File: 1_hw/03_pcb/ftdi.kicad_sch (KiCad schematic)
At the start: 32 parts, among them U4 93LC56BT-I_OT, Y3 12 MHz

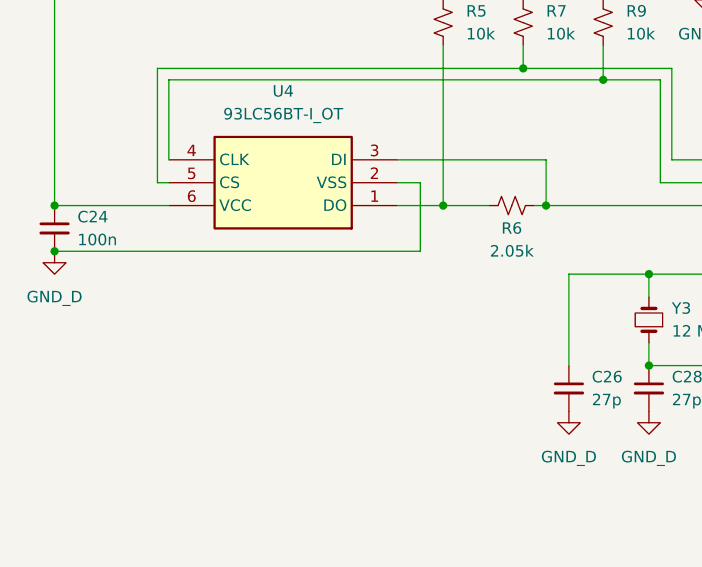
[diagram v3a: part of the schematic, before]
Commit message: FEAT: Added Analog Stage 2 to Schematic. Some additional symbols (Pot, SPDT Analog MUX, etc.) added to Project.
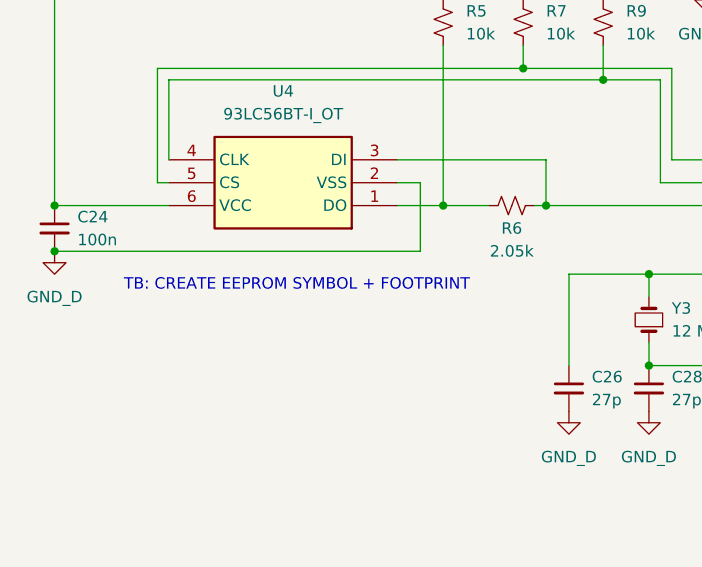
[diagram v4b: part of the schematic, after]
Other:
- note added: "TB: CREATE EEPROM SYMBOL + FOOTPRINT"
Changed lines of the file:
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@@
 		)
 	)
+	(text "TB: CREATE EEPROM SYMBOL + FOOTPRINT"
+		(exclude_from_sim no)
+		(at 71.374 134.62 0)
+		(effects
+			(font
+				(size 1.27 1.27)
+			)
+		)
+	)
 	(text "FTDI PIN 16: UART_FTDI_TXD\nFTDI PIN 17: UART_TFDI_RXD\n(LINES FLIPPED TO MCU)"
 		(exclude_from_sim no)
@@
 			)
 		)
-		(property "Description" ""
+		(property "Description" "Two pin crystal, small symbol"
 			(at 110.49 138.43 0)
 			(effects
@@
 			)
 		)
-		(property "Description" ""
+		(property "Description" "Unpolarized capacitor, small symbol"
 			(at 44.45 128.27 0)
 			(effects
@@
 			)
 		)
-		(property "Description" ""
+		(property "Description" "Unpolarized capacitor, small symbol"
 			(at 210.82 34.29 0)
 			(effects
@@
 			)
 		)
-		(property "Description" ""
+		(property "Description" "Unpolarized capacitor, small symbol"
 			(at 113.03 38.1 0)
 			(effects
@@
 			)
 		)
-		(property "Description" ""
+		(property "Description" "Unpolarized capacitor, small symbol"
 			(at 118.11 63.5 0)
 			(effects
@@
 			)
 		)
-		(property "Description" ""
+		(property "Description" "Light emitting diode"
 			(at 233.68 64.77 0)
 			(effects
@@
 			)
 		)
-		(property "Description" ""
+		(property "Description" "Unpolarized capacitor, small symbol"
 			(at 102.87 38.1 0)
 			(effects
@@
 			)
 		)
-		(property "Description" ""
+		(property "Description" "Unpolarized capacitor, small symbol"
 			(at 180.34 34.29 0)
 			(effects
@@
 			)
 		)
-		(property "Description" ""
+		(property "Description" "Unpolarized capacitor, small symbol"
 			(at 241.3 34.29 0)
 			(effects
@@
 			)
 		)
-		(property "Description" ""
+		(property "Description" "Unpolarized capacitor, small symbol"
 			(at 220.98 34.29 0)
 			(effects
@@
 			)
 		)
-		(property "Description" ""
+		(property "Description" "Unpolarized capacitor, small symbol"
 			(at 123.19 38.1 0)
 			(effects
@@
 			)
 		)
-		(property "Description" ""
+		(property "Description" "Unpolarized capacitor, small symbol"
 			(at 110.49 146.05 0)
 			(effects
@@
 			)
 		)
-		(property "Description" ""
+		(property "Description" "Inductor, small symbol"
 			(at 85.09 34.29 0)
 			(effects
@@
 			)
 		)
-		(property "Description" ""
+		(property "Description" "Unpolarized capacitor, small symbol"
 			(at 92.71 38.1 0)
 			(effects
@@
 			)
 		)
-		(property "Description" ""
+		(property "Description" "Unpolarized capacitor, small symbol"
 			(at 101.6 146.05 0)
 			(effects
@@
 			)
 		)
-		(property "Description" ""
+		(property "Description" "Inductor, small symbol"
 			(at 97.79 31.75 0)
 			(effects
@@
 			)
 		)
-		(property "Description" ""
+		(property "Description" "Unpolarized capacitor, small symbol"
 			(at 200.66 34.29 0)
 			(effects
@@
 			)
 		)
-		(property "Description" ""
+		(property "Description" "Unpolarized capacitor, small symbol"
 			(at 190.5 34.29 0)
 			(effects
@@
 			)
 		)
-		(property "Description" ""
+		(property "Description" "Light emitting diode"
 			(at 223.52 64.77 0)
 			(effects
@@
 			)
 		)
-		(property "Description" ""
+		(property "Description" "Unpolarized capacitor, small symbol"
 			(at 231.14 34.29 0)
 			(effects

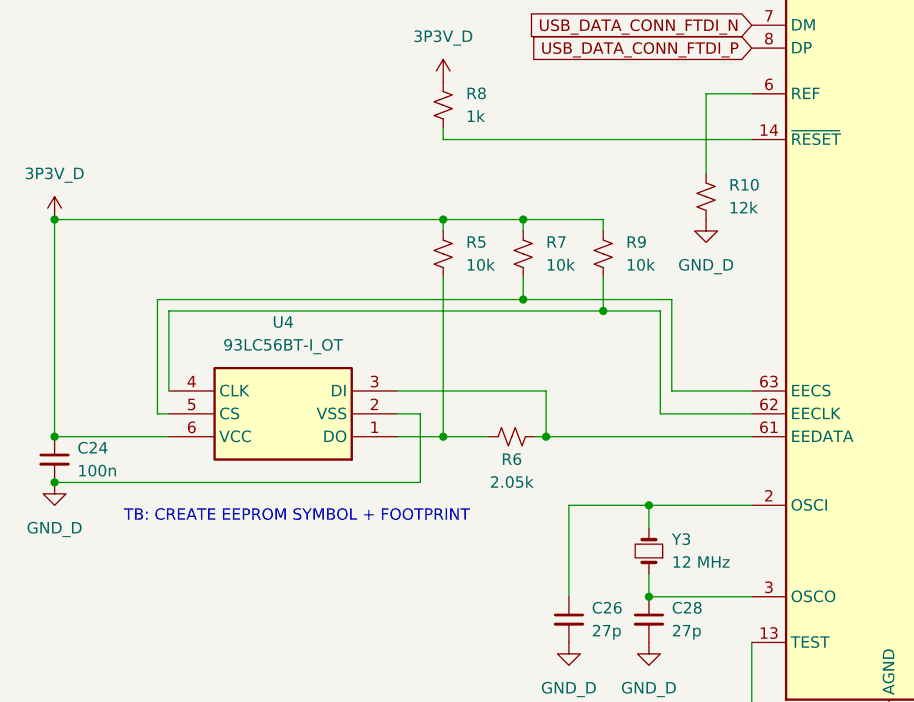
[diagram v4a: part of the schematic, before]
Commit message: FEAT: Created Power Consumption Matrix.
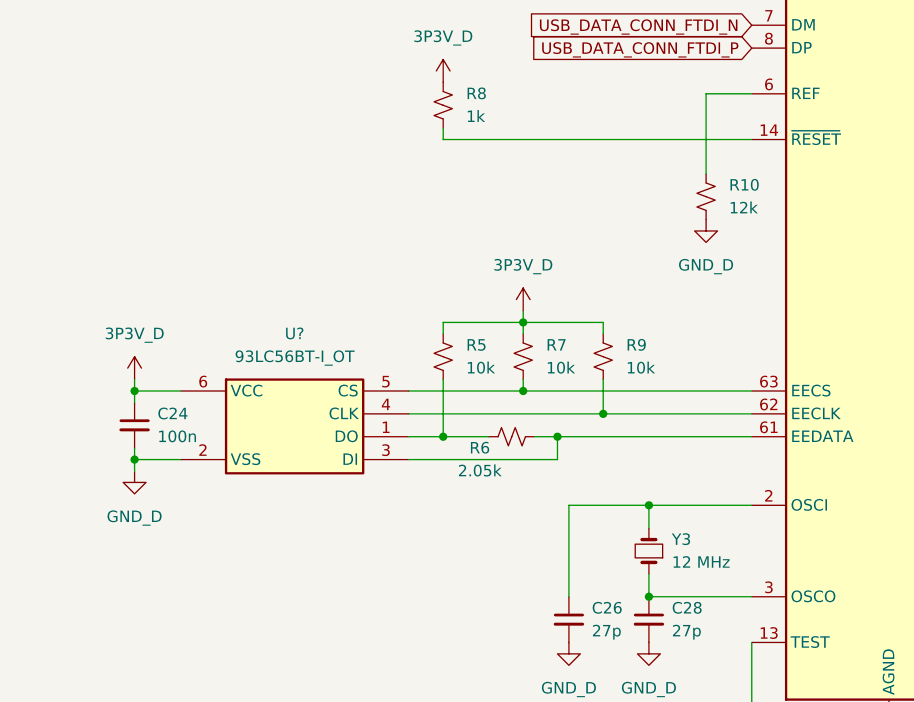
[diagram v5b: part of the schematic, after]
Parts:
- removed U4: 93LC56BT-I_OT, SOT95P270X145-6N, symbol 93LC56BT-I_OT:93LC56BT-I_OT
- removed U?: FT2232HL, Package_QFP:LQFP-64_10x10mm_P0.5mm, symbol BRZK_FTDI:FT2232HL
- added U?: 93LC56BT-I_OT, SOT95P270X145-6N, symbol BRZK_MEMORY:93LC56BT-I_OT
- added U?: FT2232HL, Package_QFP:LQFP-64_10x10mm_P0.5mm, symbol BRZK_FTDI:FT2232HL
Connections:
- net 1P8V_D: now also U?.12 (VCORE), U?.37 (VCORE), U?.49 (VREGOUT), U?.64 (VCORE)
- net 3P3V_D: now also U?.20 (VCCIO), U?.31 (VCCIO), U?.42 (VCCIO), U?.50 (VREGIN), U?.56 (VCCIO), U?.6 (VCC)
- net GND_D: now also U?.1 (GND), U?.10 (AGND), U?.11 (GND), U?.13 (TEST), U?.15 (GND), U?.2 (VSS), U?.25 (GND), U?.35 (GND), U?.47 (GND), U?.5 (GND), U?.51 (GND)
- net GPIO_UART_RXLED_FTDI_L: now also U?.29 (ACBUS3)
- net GPIO_UART_TXLED_FTDI_L: now also U?.30 (ACBUS4)
- net JTAG_FTDI_TCK_3P3: now also U?.38 (BDBUS0)
- net JTAG_FTDI_TDI_3P3: now also U?.39 (BDBUS1)
- net JTAG_FTDI_TDO_3P3: now also U?.40 (BDBUS2)
- net JTAG_FTDI_TMS_3P3: now also U?.41 (BDBUS3)
- net UART_FTDITX_MCURX_3P3: now also U?.16 (ADBUS0)
- net UART_MCUTX_FTDIRX_3P3: now also U?.17 (ADBUS1)
- net USB_DATA_CONN_FTDI_N: now also U?.7 (DM)
- net USB_DATA_CONN_FTDI_P: now also U?.8 (DP)
- net at R10.1: now also U?.6 (REF)
- net at C28.1, Y3.1: now also U?.3 (OSCO)
- net at C26.1, Y3.2: now also U?.2 (OSCI)
- net at C25.1, C27.1, C29.1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: now also U?.4 (VPHY), U?.9 (VPLL)
- net at R9.2: now also U?.4 (CLK), U?.62 (EECLK)
- net at R7.2: now also U?.5 (CS), U?.63 (EECS)
- net at R8.2: now also U?.14 (~{RESET})
- net at R5.2, R6.2: now also U?.1 (DO)
- net at R6.1: now also U?.3 (DI), U?.61 (EEDATA)
- net at R11.2, R12.1: now also U?.59 (BCBUS7)
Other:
- note removed: "TB: CREATE EEPROM SYMBOL + FOOTPRINT"
- moved on the sheet: C24, R5, R7, R9

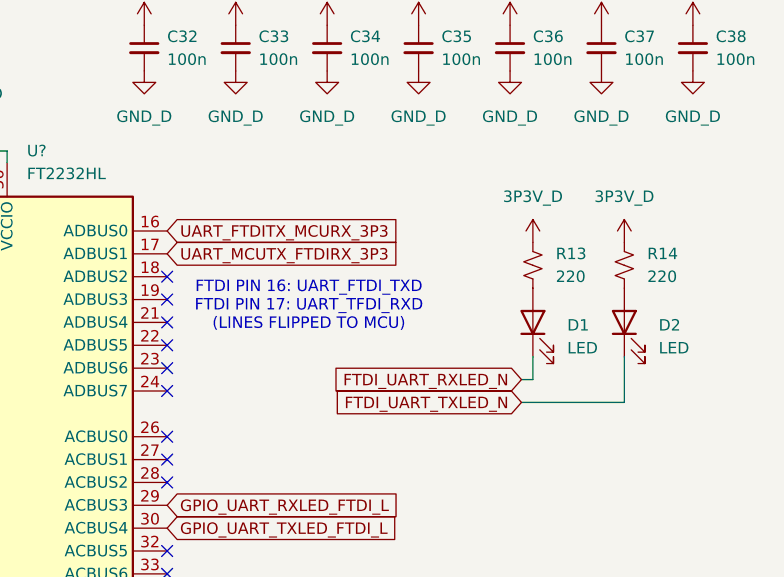
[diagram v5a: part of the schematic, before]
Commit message: FEAT: Added MCU Resources for Analog Muxing, Additional DAC, ADC, and I2C for Digital Pot. Also changed SPI Resource from 1 to 2.
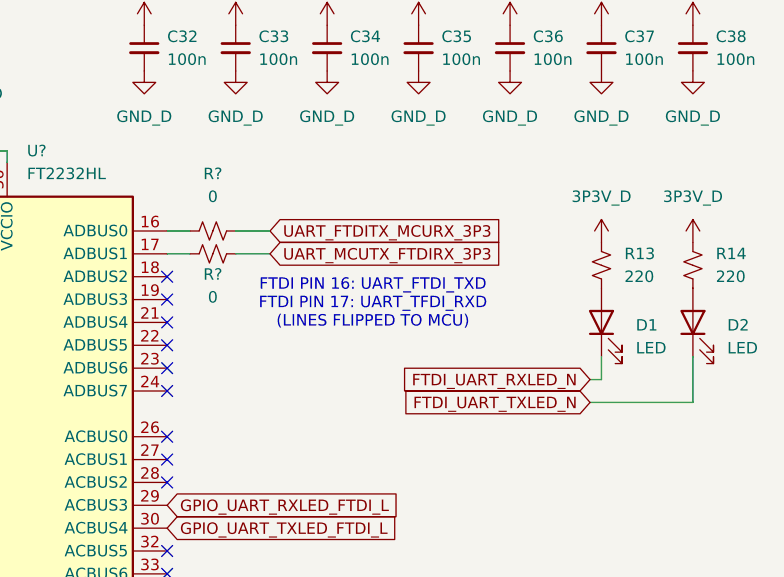
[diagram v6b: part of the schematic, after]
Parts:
- added R? (x2): 0, Resistor_SMD:R_0603_1608Metric, symbol Device:R_Small_US
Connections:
- net UART_FTDITX_MCURX_3P3: now also R?.2; no longer U?.16 (ADBUS0)
- net UART_MCUTX_FTDIRX_3P3: now also R?.2; no longer U?.17 (ADBUS1)
- new net: R?.1, U?.16 (ADBUS0)
- new net: R?.1, U?.17 (ADBUS1)
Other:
- moved on the sheet: D1, D2, R13, R14

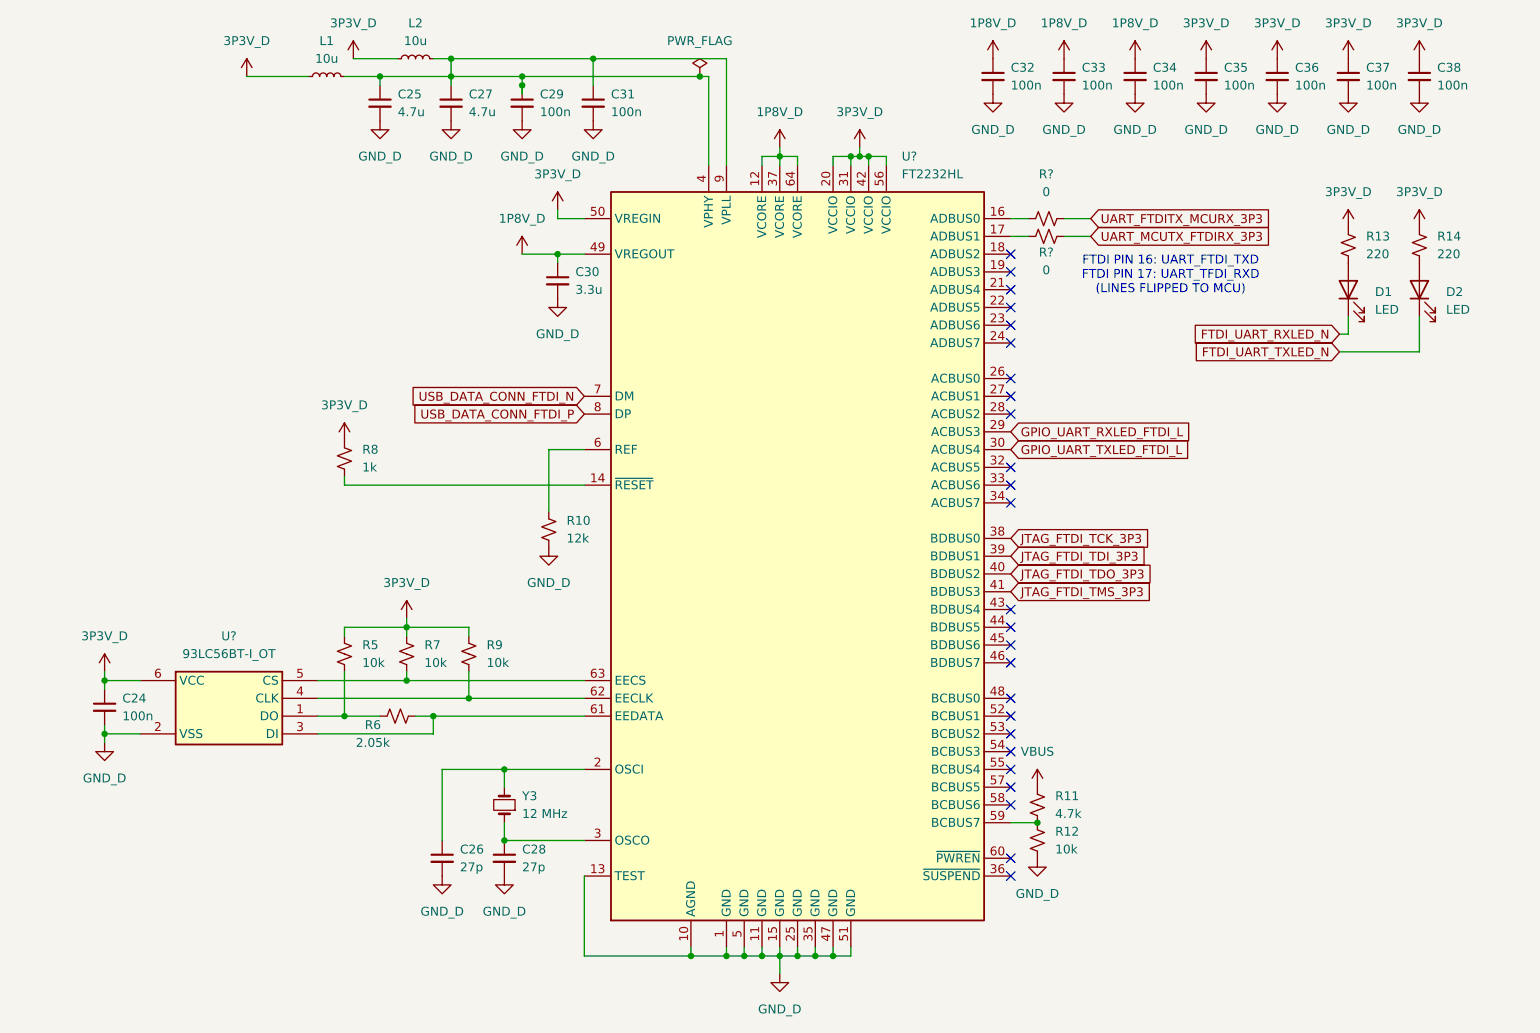
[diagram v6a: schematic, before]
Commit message: FEAT: Changed from two grounds (Digital + Analog) to Singular Ground IAW recommended Grounding Scheme.
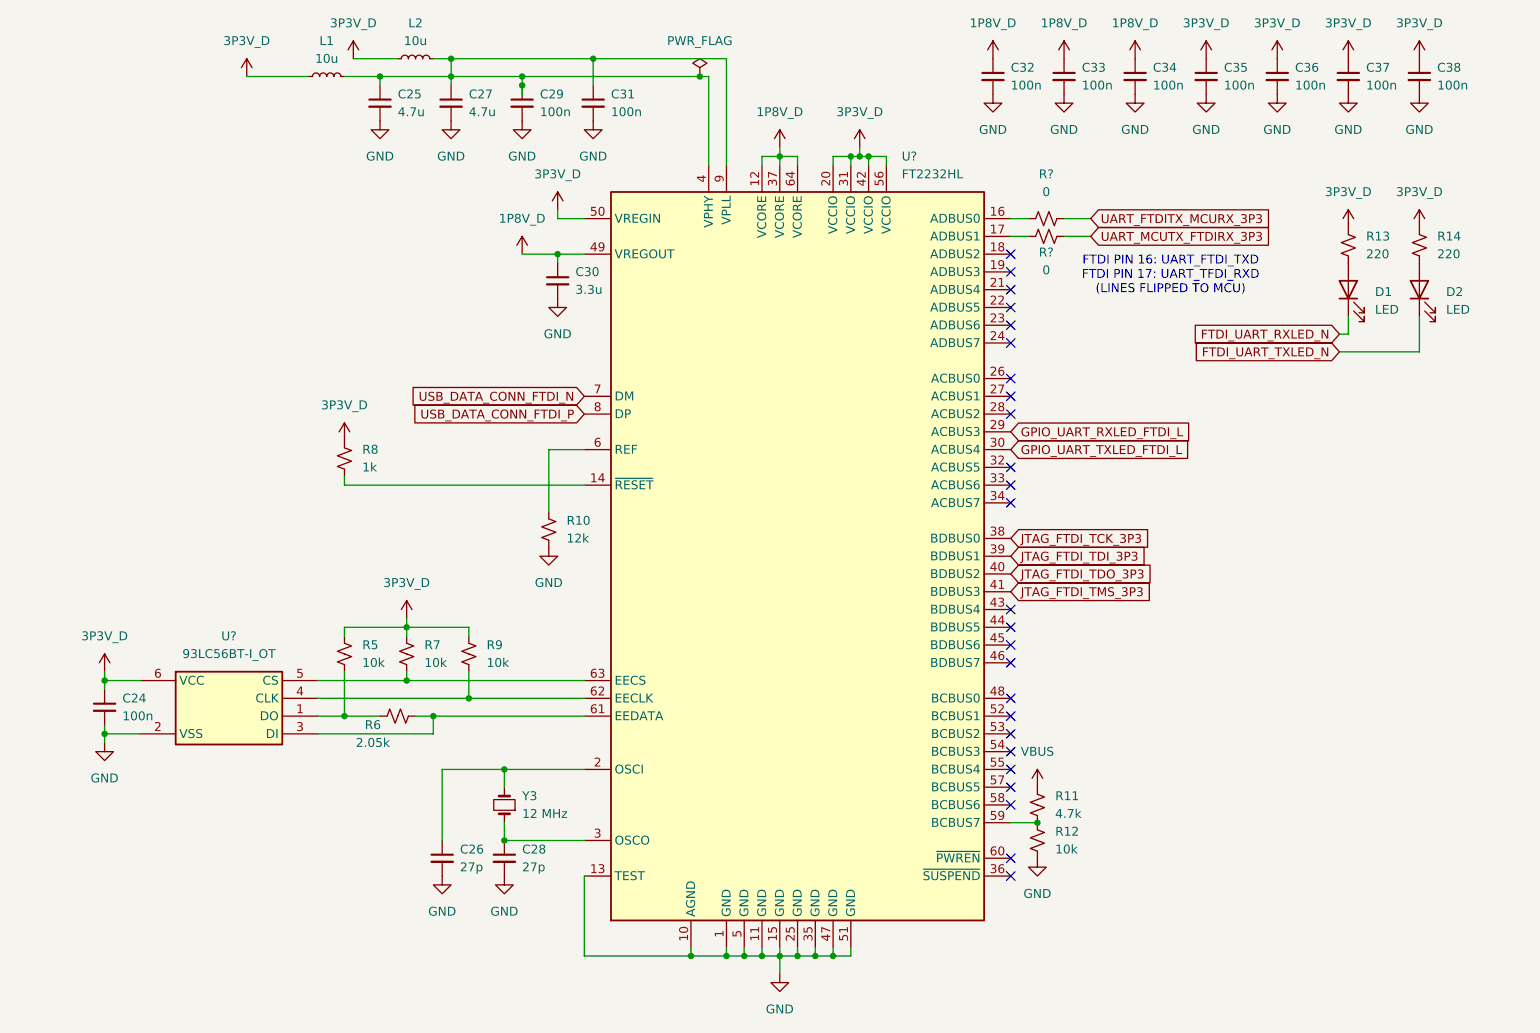
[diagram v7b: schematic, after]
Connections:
- net GND_D renamed GND
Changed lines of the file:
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@@
 			)
 		)
-		(property "Value" "GND_D"
+		(property "Value" "GND"
 			(at 231.14 41.91 0)
 			(effects
@@
 			)
 		)
-		(property "Value" "GND_D"
+		(property "Value" "GND"
 			(at 118.11 71.12 0)
 			(effects
@@
 			)
 		)
-		(property "Value" "GND_D"
+		(property "Value" "GND"
 			(at 110.49 153.67 0)
 			(effects
@@
 			)
 		)
-		(property "Value" "GND_D"
+		(property "Value" "GND"
 			(at 53.34 134.62 0)
 			(effects
@@
 			)
 		)
-		(property "Value" "GND_D"
+		(property "Value" "GND"
 			(at 102.87 45.72 0)
 			(effects
@@
 			)
 		)
-		(property "Value" "GND_D"
+		(property "Value" "GND"
 			(at 190.5 41.91 0)
 			(effects
@@
 			)
 		)
-		(property "Value" "GND_D"
+		(property "Value" "GND"
 			(at 200.66 41.91 0)
 			(effects
@@
 			)
 		)
-		(property "Value" "GND_D"
+		(property "Value" "GND"
 			(at 210.82 41.91 0)
 			(effects
@@
 			)
 		)
-		(property "Value" "GND_D"
+		(property "Value" "GND"
 			(at 113.03 45.72 0)
 			(effects
@@
 			)
 		)
-		(property "Value" "GND_D"
+		(property "Value" "GND"
 			(at 149.86 167.64 0)
 			(effects
@@
 			)
 		)
-		(property "Value" "GND_D"
+		(property "Value" "GND"
 			(at 186.69 151.13 0)
 			(effects
@@
 			)
 		)
-		(property "Value" "GND_D"
+		(property "Value" "GND"
 			(at 180.34 41.91 0)
 			(effects
@@
 			)
 		)
-		(property "Value" "GND_D"
+		(property "Value" "GND"
 			(at 92.71 45.72 0)
 			(effects
@@
 			)
 		)
-		(property "Value" "GND_D"
+		(property "Value" "GND"
 			(at 123.19 45.72 0)
 			(effects
@@
 			)
 		)
-		(property "Value" "GND_D"
+		(property "Value" "GND"
 			(at 101.6 153.67 0)
 			(effects
@@
 			)
 		)
-		(property "Value" "GND_D"
+		(property "Value" "GND"
 			(at 116.84 106.68 0)
 			(effects
@@
 			)
 		)
-		(property "Value" "GND_D"
+		(property "Value" "GND"
 			(at 241.3 41.91 0)
 			(effects
@@
 			)
 		)
-		(property "Value" "GND_D"
+		(property "Value" "GND"
 			(at 220.98 41.91 0)
 			(effects

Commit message: FEAT: Added +15V and -15V Regulator. Replaced some Symbols to add additional Part Number Field.
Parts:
- U?: Part Number (none) -> 93LC56BT-I_OT
- U?: Part Number (none) -> FT2232HL
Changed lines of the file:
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@@
+			)
+		)
+		(property "Part Number" "93LC56BT-I_OT"
+			(at 71.12 118.11 0)
+			(effects
+				(font
+					(size 1.27 1.27)
+				)
+				(hide yes)
 			)
 		)
@@
 			(at 152.4 102.87 0)
 			(effects
+				(font
+					(size 1.27 1.27)
+				)
+				(hide yes)
+			)
+		)
+		(property "Part Number" "FT2232HL"
+			(at 152.4 102.87 0)
+			(effects
